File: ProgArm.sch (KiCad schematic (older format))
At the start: 129 parts, among them K1 RING_LEDS, M1 MOTOR, P1 I²C_Port, P10 RING_VCC, P11 RING_GND, P12 RING_GPIO_1, P13 GPIOA_Port_1, P14 RXD, P15 RING_BUTTONS, P16 MicroUSB, P2 SPI_Port, P3 UART_Port, P4 SWD_Interface, P5 GPIOA_Port_1_2, P6 TIM1_Port, P7 T_SENS, P8 RING_IR_OUT, P9 TXD, Q1 MOS_P, Q2 MOS_P, Q3 MOS_P, Q4 MOS_P, Q5 MOS_P, Q6 MOS_P, Q7 MOS_P, Q8 MOS_P, SW1 ON/OFF, U1 TPS78330, U2 BQ24297, U3 LM3668, U4 STM32F103R, U5 MPU9250, U6 BQ27410, U7 SI1143, U8 LPS25H, U9 NRF8001, X1 32.768(MS3V-T1R), X2 8MHz, X3 16MHz

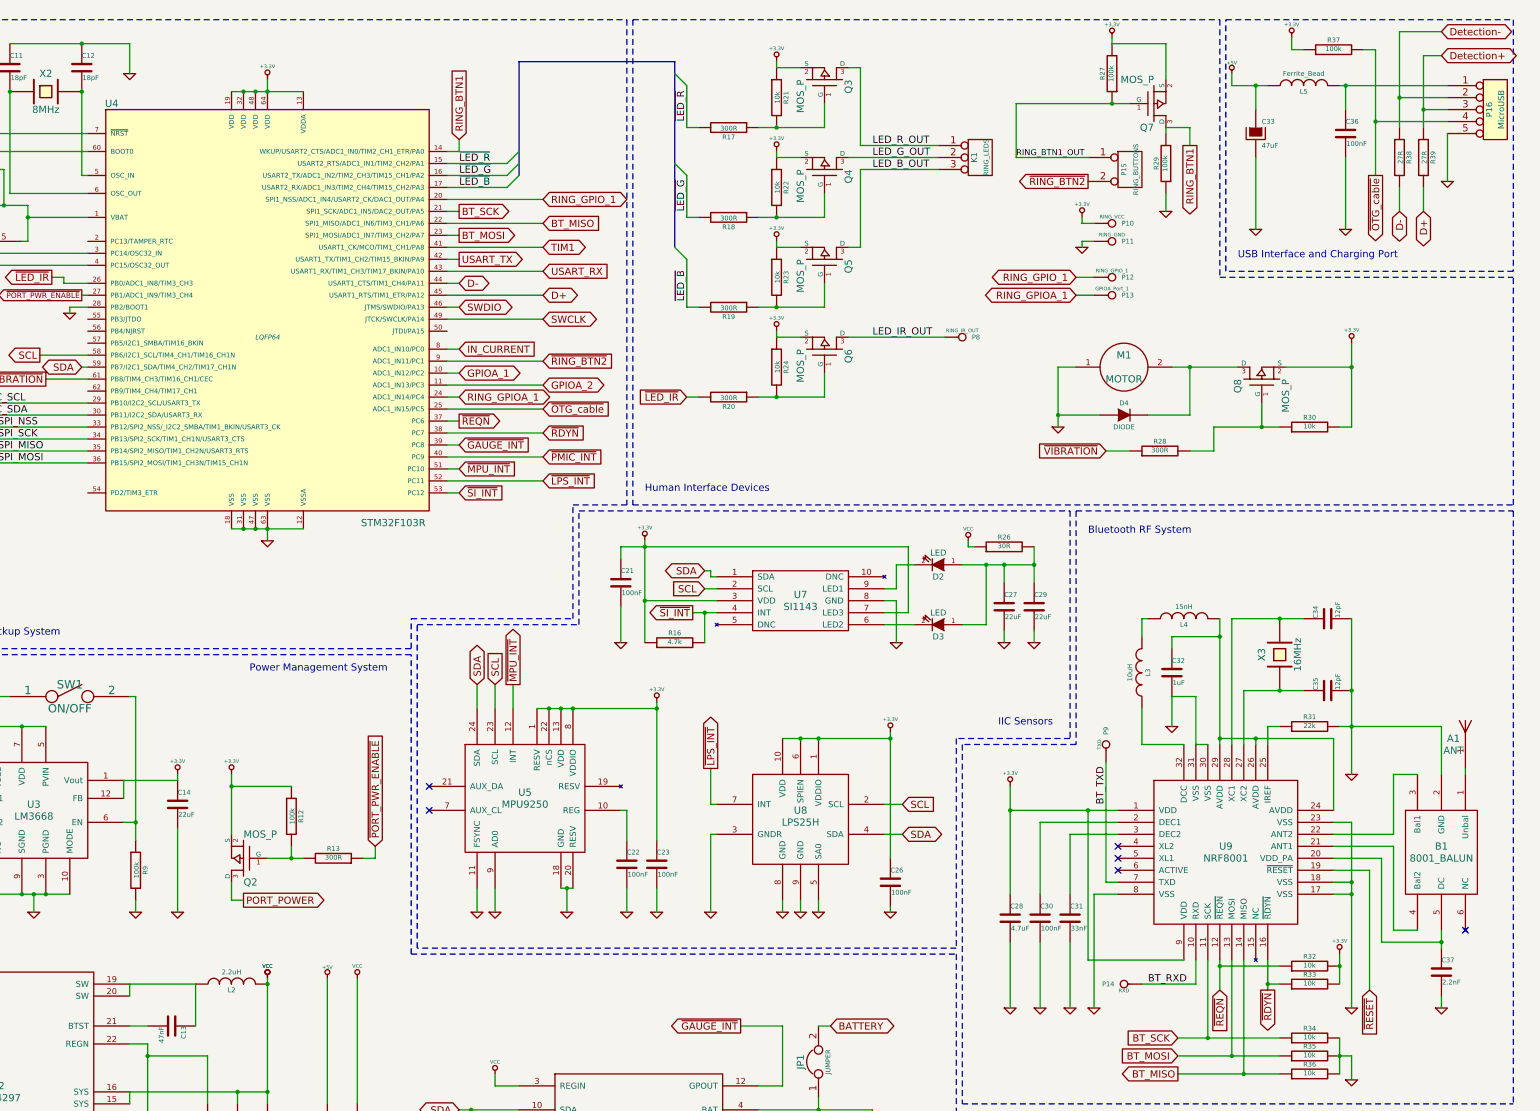
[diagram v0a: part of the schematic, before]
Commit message: Managed ERC Test pass
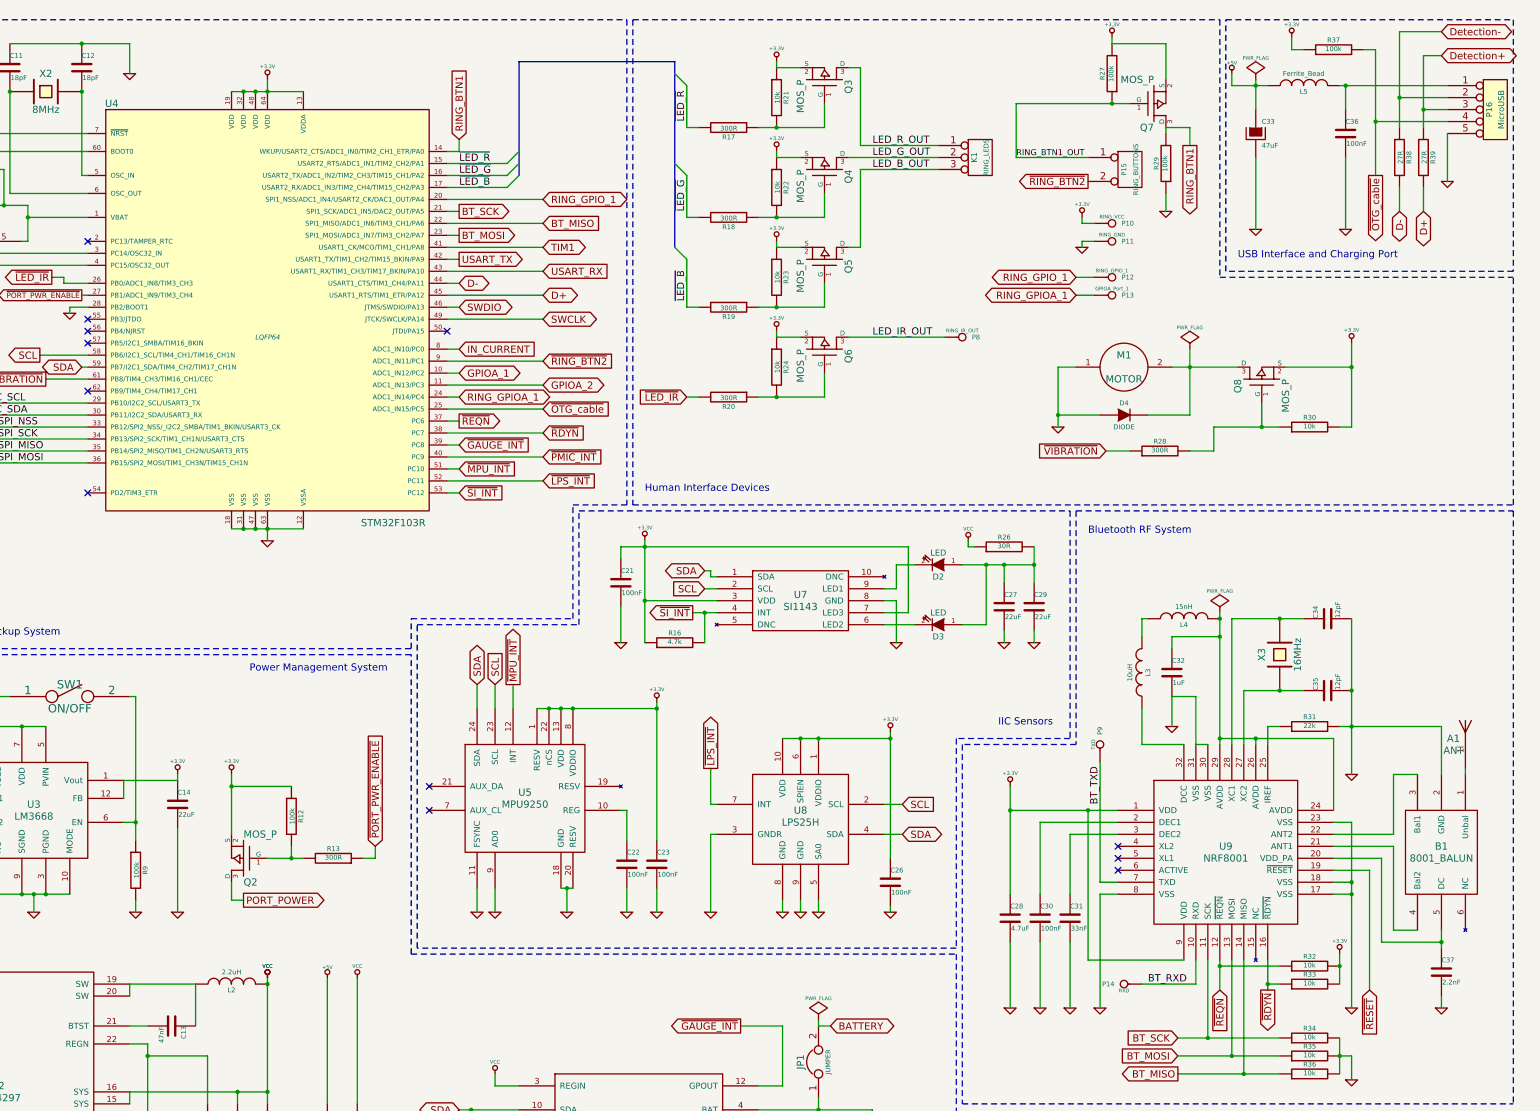
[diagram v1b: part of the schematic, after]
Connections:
- no-connect marks 7 -> 13
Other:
- moved on the sheet: P9
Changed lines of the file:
@@
 	3450 750  4450 750
 Wire Wire Line
-	13300 3450 13300 3850
+	13300 3300 13300 3850
 Wire Wire Line
 	13150 3450 13700 3450
@@
 	14600 1300 14600 1100
 Wire Wire Line
-	13850 1300 13850 1100
+	13850 1050 13850 1300
 Connection ~ 13850 1100
 Wire Wire Line
@@
 	12900 6300 12900 6600
 Wire Wire Line
-	13550 5550 13550 6600
+	13550 5500 13550 6600
 Wire Wire Line
 	14500 6550 14500 7150
@@
 Wire Wire Line
 	15400 6450 15400 6850
-NoConn ~ 15600 8150
 $Comp
 L ANT A1
@@
 L GND #PWR077
 U 1 1 547E7A95
-P 12500 8800
-F 0 "#PWR077" H 12500 8800 30  0001 C CNN
-F 1 "GND" H 12500 8730 30  0001 C CNN
-F 2 "" H 12500 8800 60  0000 C CNN
-F 3 "" H 12500 8800 60  0000 C CNN
-	1    12500 8800
-	1    0    0    -1
-$EndComp
-Wire Wire Line
-	12700 7850 12500 7850
-Wire Wire Line
-	12500 7850 12500 8800
+P 12550 8800
+F 0 "#PWR077" H 12550 8800 30  0001 C CNN
+F 1 "GND" H 12550 8730 30  0001 C CNN
+F 2 "" H 12550 8800 60  0000 C CNN
+F 3 "" H 12550 8800 60  0000 C CNN
+	1    12550 8800
+	1    0    0    -1
+$EndComp
+Wire Wire Line
+	12550 7850 12550 8800
 NoConn ~ 12700 7650
 Wire Wire Line
@@
 BT_SCK
 Wire Wire Line
-	12700 7750 12600 7750
+	12550 7750 12700 7750
 $Comp
 L CONN_1 P14
@@
 L CONN_1 P9
 U 1 1 547E9AF8
-P 12600 6600
-F 0 "P9" H 12680 6600 40  0000 L CNN
-F 1 "TXD" H 12600 6655 30  0000 C CNN
-F 2 "" H 12600 6600 60  0000 C CNN
-F 3 "" H 12600 6600 60  0000 C CNN
-	1    12600 6600
+P 12550 6600
+F 0 "P9" H 12630 6600 40  0000 L CNN
+F 1 "TXD" H 12550 6655 30  0000 C CNN
+F 2 "" H 12550 6600 60  0000 C CNN
+F 3 "" H 12550 6600 60  0000 C CNN
+	1    12550 6600
 	0    -1   -1   0
 $EndComp
@@
 	11850 1700 12450 1700
 Wire Wire Line
-	12600 7750 12600 6750
-Text Label 12600 7100 1    60   ~ 0
+	12550 7750 12550 6750
+Text Label 12550 7100 1    60   ~ 0
 BT_TXD
 Text Label 12950 8600 0    60   ~ 0
@@
 Wire Wire Line
 	11450 4950 11500 4950
+Wire Wire Line
+	12550 7850 12700 7850
+NoConn ~ 4100 2400
+NoConn ~ 4100 3050
+NoConn ~ 4100 3150
+NoConn ~ 4100 3250
+NoConn ~ 4100 3650
+NoConn ~ 4100 4500
+NoConn ~ 7100 3150
+$Comp
+L PWR_FLAG #FLG098
+U 1 1 548623D3
+P 13850 1050
+F 0 "#FLG098" H 13850 1145 30  0001 C CNN
+F 1 "PWR_FLAG" H 13850 1230 30  0000 C CNN
+F 2 "" H 13850 1050 60  0000 C CNN
+F 3 "" H 13850 1050 60  0000 C CNN
+	1    13850 1050
+	1    0    0    -1
+$EndComp
+$Comp
+L PWR_FLAG #FLG099
+U 1 1 54862897
+P 13550 5500
+F 0 "#FLG099" H 13550 5595 30  0001 C CNN
+F 1 "PWR_FLAG" H 13550 5680 30  0000 C CNN
+F 2 "" H 13550 5500 60  0000 C CNN
+F 3 "" H 13550 5500 60  0000 C CNN
+	1    13550 5500
+	1    0    0    -1
+$EndComp
+Connection ~ 13550 5550
+$Comp
+L PWR_FLAG #FLG0100
+U 1 1 54862AFC
+P 10200 8900
+F 0 "#FLG0100" H 10200 8995 30  0001 C CNN
+F 1 "PWR_FLAG" H 10200 9080 30  0000 C CNN
+F 2 "" H 10200 8900 60  0000 C CNN
+F 3 "" H 10200 8900 60  0000 C CNN
+	1    10200 8900
+	1    0    0    -1
+$EndComp
+Wire Wire Line
+	10200 8950 10200 8900
+$Comp
+L PWR_FLAG #FLG0101
+U 1 1 54862FDC
+P 13300 3300
+F 0 "#FLG0101" H 13300 3395 30  0001 C CNN
+F 1 "PWR_FLAG" H 13300 3480 30  0000 C CNN
+F 2 "" H 13300 3300 60  0000 C CNN
+F 3 "" H 13300 3300 60  0000 C CNN
+	1    13300 3300
+	1    0    0    -1
+$EndComp
 $EndSCHEMATC

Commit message: We have passed ERC Test!
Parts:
- added R9: 10k, ~, symbol R
- renumbered R9 to R10, R10 to R11, R11 to R12, R12 to R13, R13 to R14, R14 to R15, R15 to R16, R16 to R17, R17 to R18, R18 to R19, R19 to R20, R20 to R21, R21 to R22, R22 to R23, R23 to R24, R24 to R25, R25 to R26, R26 to R27, R27 to R28, R28 to R29, R29 to R30, R30 to R31, R31 to R32, R32 to R33, R33 to R34, R34 to R35, R35 to R36, R36 to R37, R37 to R38, R38 to R39, R39 to R40
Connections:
- net GND: now also R9.1; no longer U4.28 (PB2/BOOT1)
- new net: R9.2, U4.28 (PB2/BOOT1)
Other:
- moved on the sheet: BT1, C20, C24, C25, JP1, R15, R16, R26, U6

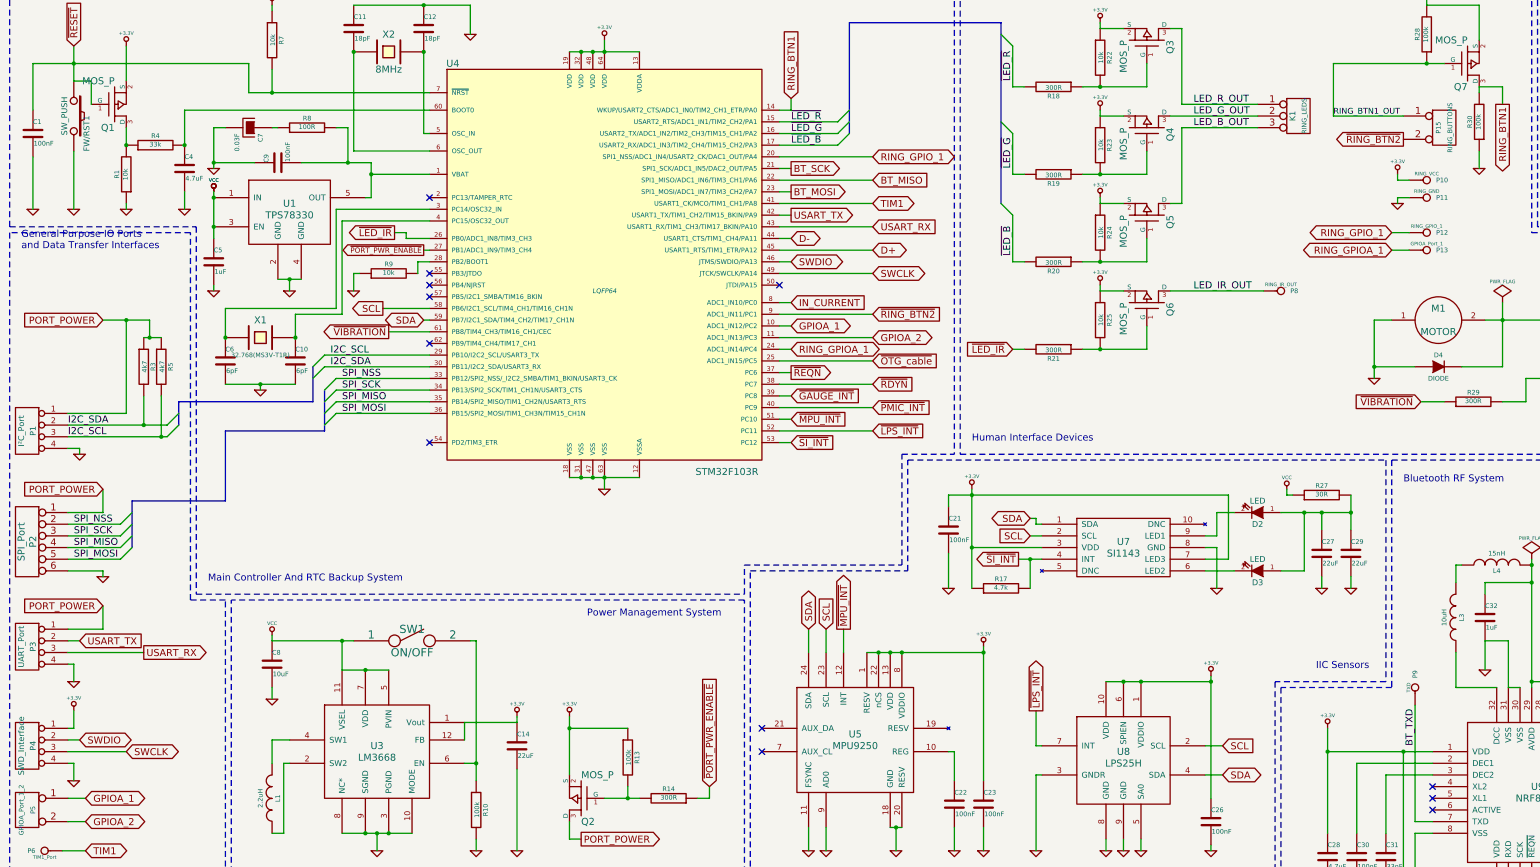
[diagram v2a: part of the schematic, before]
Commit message: Components numeration, description fixes
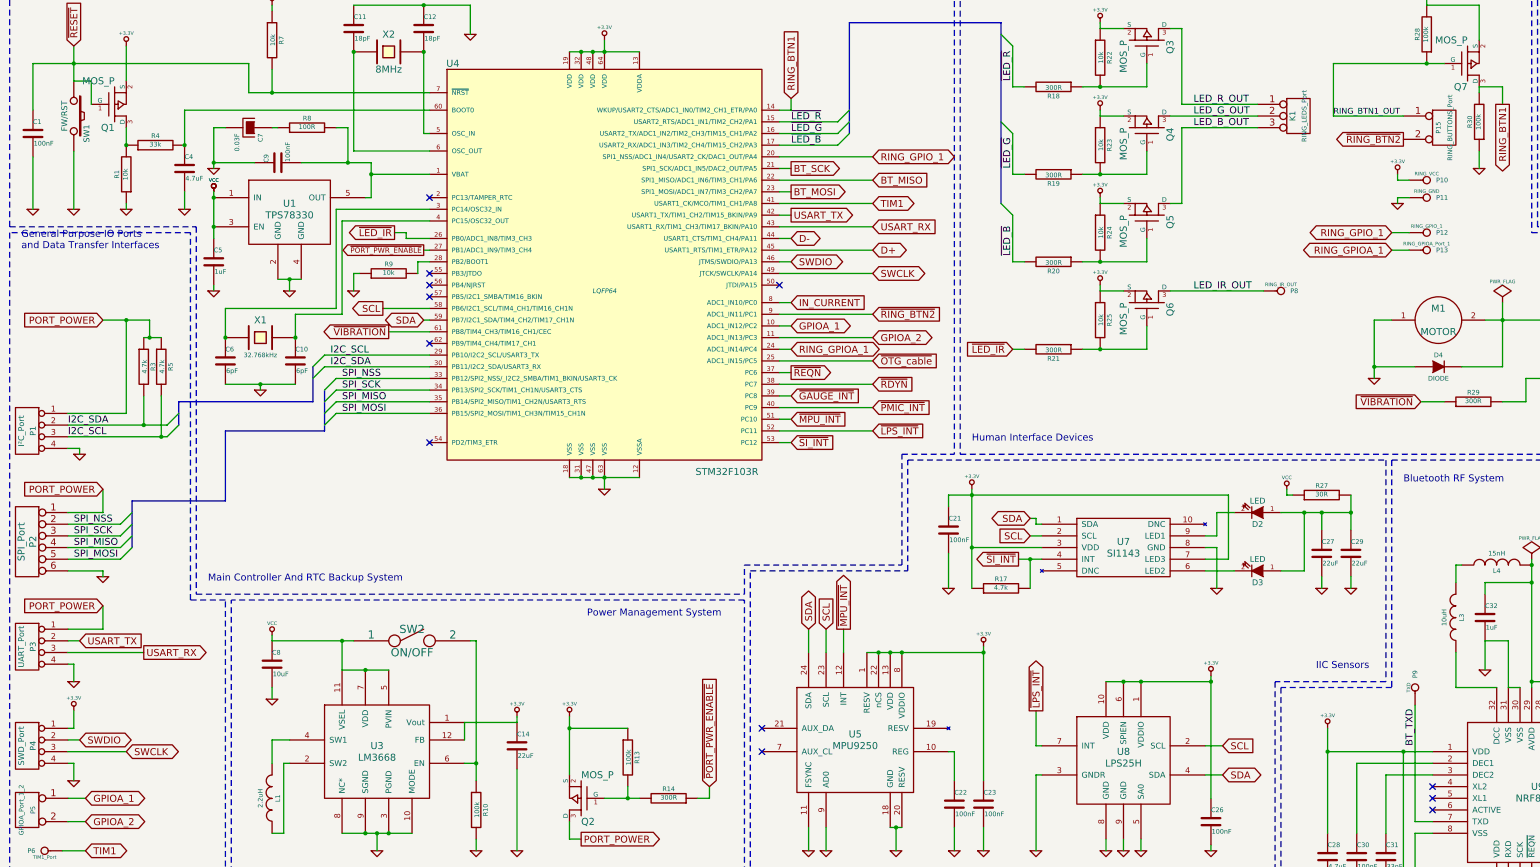
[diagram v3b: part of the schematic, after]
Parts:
- K1: value RING_LEDS -> RING_LEDS_Port
- P13: value GPIOA_Port_1 -> RING_GPIOA_Port_1
- P15: value RING_BUTTONS -> RING_BUTTONS_Port
- P4: value SWD_Interface -> SWD_Port
- R3, R5: value 4k7 -> 4.7k
- SW1: renamed from FW/RST1; value SW_PUSH -> FW/RST
- X1: value 32.768(MS3V-T1R) -> 32.768kHz
- renumbered SW1 to SW2

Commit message: Ports managed
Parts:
- P12: value RING_GPIO_1 -> RING_GPIOA_4_Port
- P13: value RING_GPIOA_Port_1 -> RING_GPIOA_3_Port
- P5: value GPIOA_Port_1_2 -> GPIOA_1_2_Port
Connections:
- net RING_GPIOA_1 renamed GPIOA_3
- net RING_GPIO_1 renamed GPIOA_4
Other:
- moved on the sheet: C26, P12, P13, U8
